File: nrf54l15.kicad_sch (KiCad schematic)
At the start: 16 parts, among them U1 nRF54L15-QDXX, X1 XL7EL89CKI-111YLC-32M

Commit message: Push current KiCad workspace changes
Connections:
- net I2C_SDA: now also U1.5 (P1.04); no longer U1.24 (P0.04)
- net PMIC_INT: now reaches U1.20 (P0.00)
- net VOUT1 renamed VOUT2
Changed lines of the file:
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@@
-	)
-	(no_connect
-		(at 109.22 88.9)
 	)
 	(no_connect
@@
 	)
 	(no_connect
+		(at 109.22 78.74)
+	)
+	(no_connect
 		(at 109.22 55.88)
 	)
@@
 	(wire
 		(pts
+			(xy 106.68 88.9) (xy 109.22 88.9)
+		)
+		(stroke
+			(width 0)
+			(type default)
+		)
+	)
+	(wire
+		(pts
 			(xy 101.6 71.12) (xy 109.22 71.12)
 		)
@@
 	(wire
 		(pts
+			(xy 82.55 63.5) (xy 106.68 63.5)
+		)
+		(stroke
+			(width 0)
+			(type default)
+		)
+	)
+	(wire
+		(pts
 			(xy 223.52 40.64) (xy 204.47 40.64)
 		)
@@
 	(wire
 		(pts
+			(xy 110.49 19.05) (xy 110.49 17.78)
+		)
+		(stroke
+			(width 0)
+			(type default)
+		)
+	)
+	(wire
+		(pts
 			(xy 191.77 30.48) (xy 191.77 29.21)
 		)
@@
 	(wire
 		(pts
+			(xy 106.68 68.58) (xy 109.22 68.58)
+		)
+		(stroke
+			(width 0)
+			(type default)
+		)
+	)
+	(wire
+		(pts
+			(xy 105.41 91.44) (xy 106.68 91.44)
+		)
+		(stroke
+			(width 0)
+			(type default)
+		)
+	)
+	(wire
+		(pts
 			(xy 165.1 93.98) (xy 172.72 93.98)
 		)
@@
 	(wire
 		(pts
+			(xy 106.68 91.44) (xy 106.68 88.9)
+		)
+		(stroke
+			(width 0)
+			(type default)
+		)
+	)
+	(wire
+		(pts
 			(xy 204.47 40.64) (xy 204.47 39.37)
 		)
@@
 	(wire
 		(pts
+			(xy 106.68 63.5) (xy 106.68 68.58)
+		)
+		(stroke
+			(width 0)
+			(type default)
+		)
+	)
+	(wire
+		(pts
 			(xy 186.69 93.98) (xy 186.69 97.79)
+		)
+		(stroke
+			(width 0)
+			(type default)
+		)
+	)
+	(wire
+		(pts
+			(xy 93.98 19.05) (xy 110.49 19.05)
 		)
 		(stroke
@@
 	(global_label "I2C_SDA"
 		(shape input)
-		(at 109.22 78.74 180)
+		(at 105.41 91.44 180)
 		(fields_autoplaced yes)
 		(effects
@@
 		)
 		(property "Intersheetrefs" "${INTERSHEET_REFS}"
-			(at 98.6148 78.74 0)
+			(at 94.8048 91.44 0)
 			(hide yes)
 			(show_name no)
@@
 		)
 	)
-	(global_label "VOUT1"
+	(global_label "nRF54_SWDCLK"
 		(shape input)
-		(at 110.49 17.78 180)
+		(at 165.1 142.24 0)
+		(fields_autoplaced yes)
+		(effects
+			(font
+				(size 1.27 1.27)
+			)
+			(justify left)
+		)
+		(property "Intersheetrefs" "${INTERSHEET_REFS}"
+			(at 182.4784 142.24 0)
+			(hide yes)
+			(show_name no)
+			(do_not_autoplace no)
+			(effects
+				(font
+					(size 1.27 1.27)
+				)
+				(justify left)
+			)
+		)
+	)
+	(global_label "nRF54_SWDIO"
+		(shape input)
+		(at 165.1 144.78 0)
+		(fields_autoplaced yes)
+		(effects
+			(font
+				(size 1.27 1.27)
+			)
+			(justify left)
+		)
+		(property "Intersheetrefs" "${INTERSHEET_REFS}"
+			(at 180.8456 144.78 0)
+			(hide yes)
+			(show_name no)
+			(do_not_autoplace no)
+			(effects
+				(font
+					(size 1.27 1.27)
+				)
+				(justify left)
+			)
+		)
+	)
+	(global_label "nRF54_RESET"
+		(shape input)
+		(at 190.5 137.16 0)
+		(fields_autoplaced yes)
+		(effects
+			(font
+				(size 1.27 1.27)
+			)
+			(justify left)
+		)
+		(property "Intersheetrefs" "${INTERSHEET_REFS}"
+			(at 206.1245 137.16 0)
+			(hide yes)
+			(show_name no)
+			(do_not_autoplace no)
+			(effects
+				(font
+					(size 1.27 1.27)
+				)
+				(justify left)
+			)
+		)
+	)
+	(global_label "ANT_SEL"
+		(shape output)
+		(at 101.6 71.12 180)
 		(fields_autoplaced yes)
 		(effects
@@
 		)
 		(property "Intersheetrefs" "${INTERSHEET_REFS}"
-			(at 101.5781 17.78 0)
+			(at 90.8739 71.12 0)
 			(hide yes)
 			(show_name no)
@@
 		)
 	)
-	(global_label "nRF54_SWDCLK"
+	(global_label "PMIC_INT"
 		(shape input)
-		(at 165.1 142.24 0)
-		(fields_autoplaced yes)
-		(effects
-			(font
-				(size 1.27 1.27)
-			)
-			(justify left)
-		)
-		(property "Intersheetrefs" "${INTERSHEET_REFS}"
-			(at 182.4784 142.24 0)
-			(hide yes)
-			(show_name no)
-			(do_not_autoplace no)
-			(effects
-				(font
-					(size 1.27 1.27)
-				)
-				(justify left)
-			)
-		)
-	)
-	(global_label "nRF54_SWDIO"
-		(shape input)
-		(at 165.1 144.78 0)
-		(fields_autoplaced yes)
-		(effects
-			(font
-				(size 1.27 1.27)
-			)
-			(justify left)
-		)
-		(property "Intersheetrefs" "${INTERSHEET_REFS}"
-			(at 180.8456 144.78 0)
-			(hide yes)
-			(show_name no)
-			(do_not_autoplace no)
-			(effects
-				(font
-					(size 1.27 1.27)
-				)
-				(justify left)
-			)
-		)
-	)
-	(global_label "nRF54_RESET"
-		(shape input)
-		(at 190.5 137.16 0)
-		(fields_autoplaced yes)
-		(effects
-			(font
-				(size 1.27 1.27)
-			)
-			(justify left)
-		)
-		(property "Intersheetrefs" "${INTERSHEET_REFS}"
-			(at 206.1245 137.16 0)
-			(hide yes)
-			(show_name no)
-			(do_not_autoplace no)
-			(effects
-				(font
-					(size 1.27 1.27)
-				)
-				(justify left)
-			)
-		)
-	)
-	(global_label "ANT_SEL"
-		(shape output)
-		(at 101.6 71.12 180)
+		(at 82.55 63.5 180)
 		(fields_autoplaced yes)
 		(effects
@@
 		)
 		(property "Intersheetrefs" "${INTERSHEET_REFS}"
-			(at 90.8739 71.12 0)
+			(at 71.0981 63.5 0)
 			(hide yes)
 			(show_name no)
@@
 			(hide yes)
 			(show_name no)
+			(do_not_autoplace no)
+			(effects
+				(font
+					(size 1.27 1.27)
+				)
+				(justify right)
+			)
+		)
+	)
+	(global_label "VOUT2"
+		(shape input)
+		(at 93.98 19.05 180)
+		(fields_autoplaced yes)
+		(effects
+			(font
+				(size 1.27 1.27)
+			)
+			(justify right)
+		)
+		(property "Intersheetrefs" "${INTERSHEET_REFS}"
+			(at 85.0681 19.05 0)
+			(hide yes)
+			(show_name no)

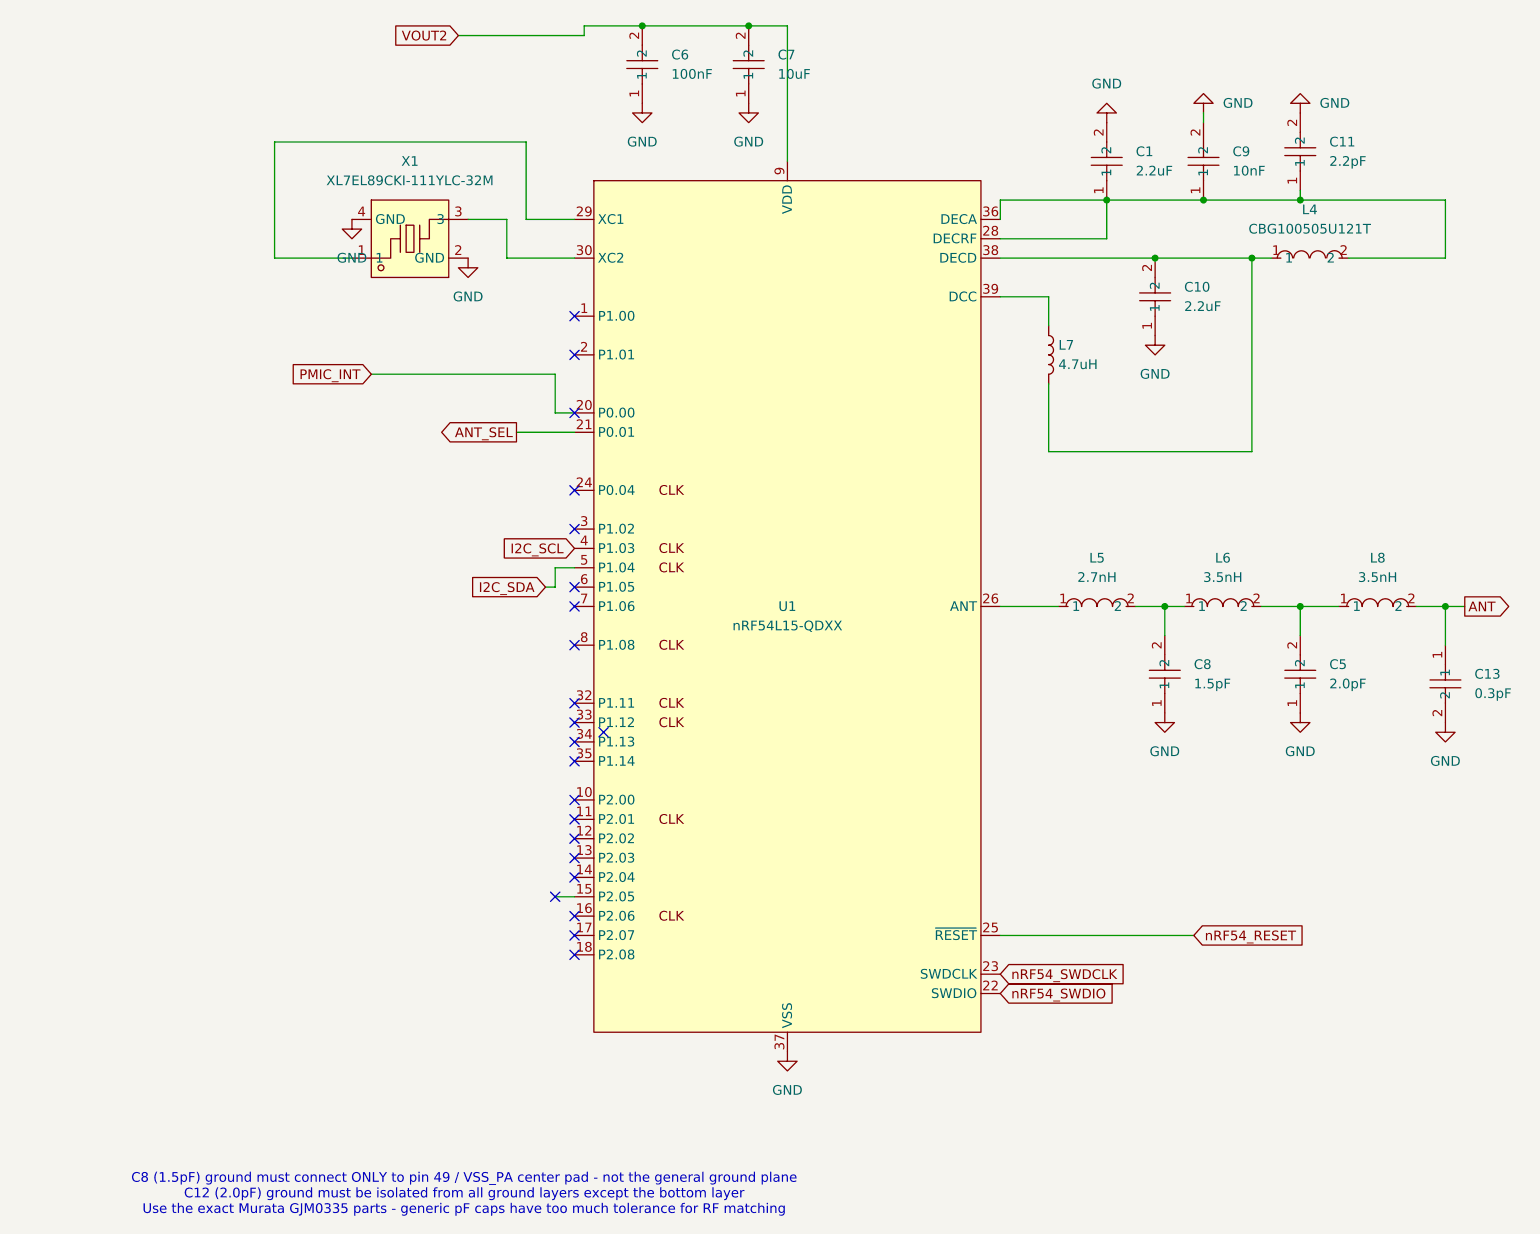
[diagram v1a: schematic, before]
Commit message: Update nRF54L15 schematic, PCB layout, and project configuration
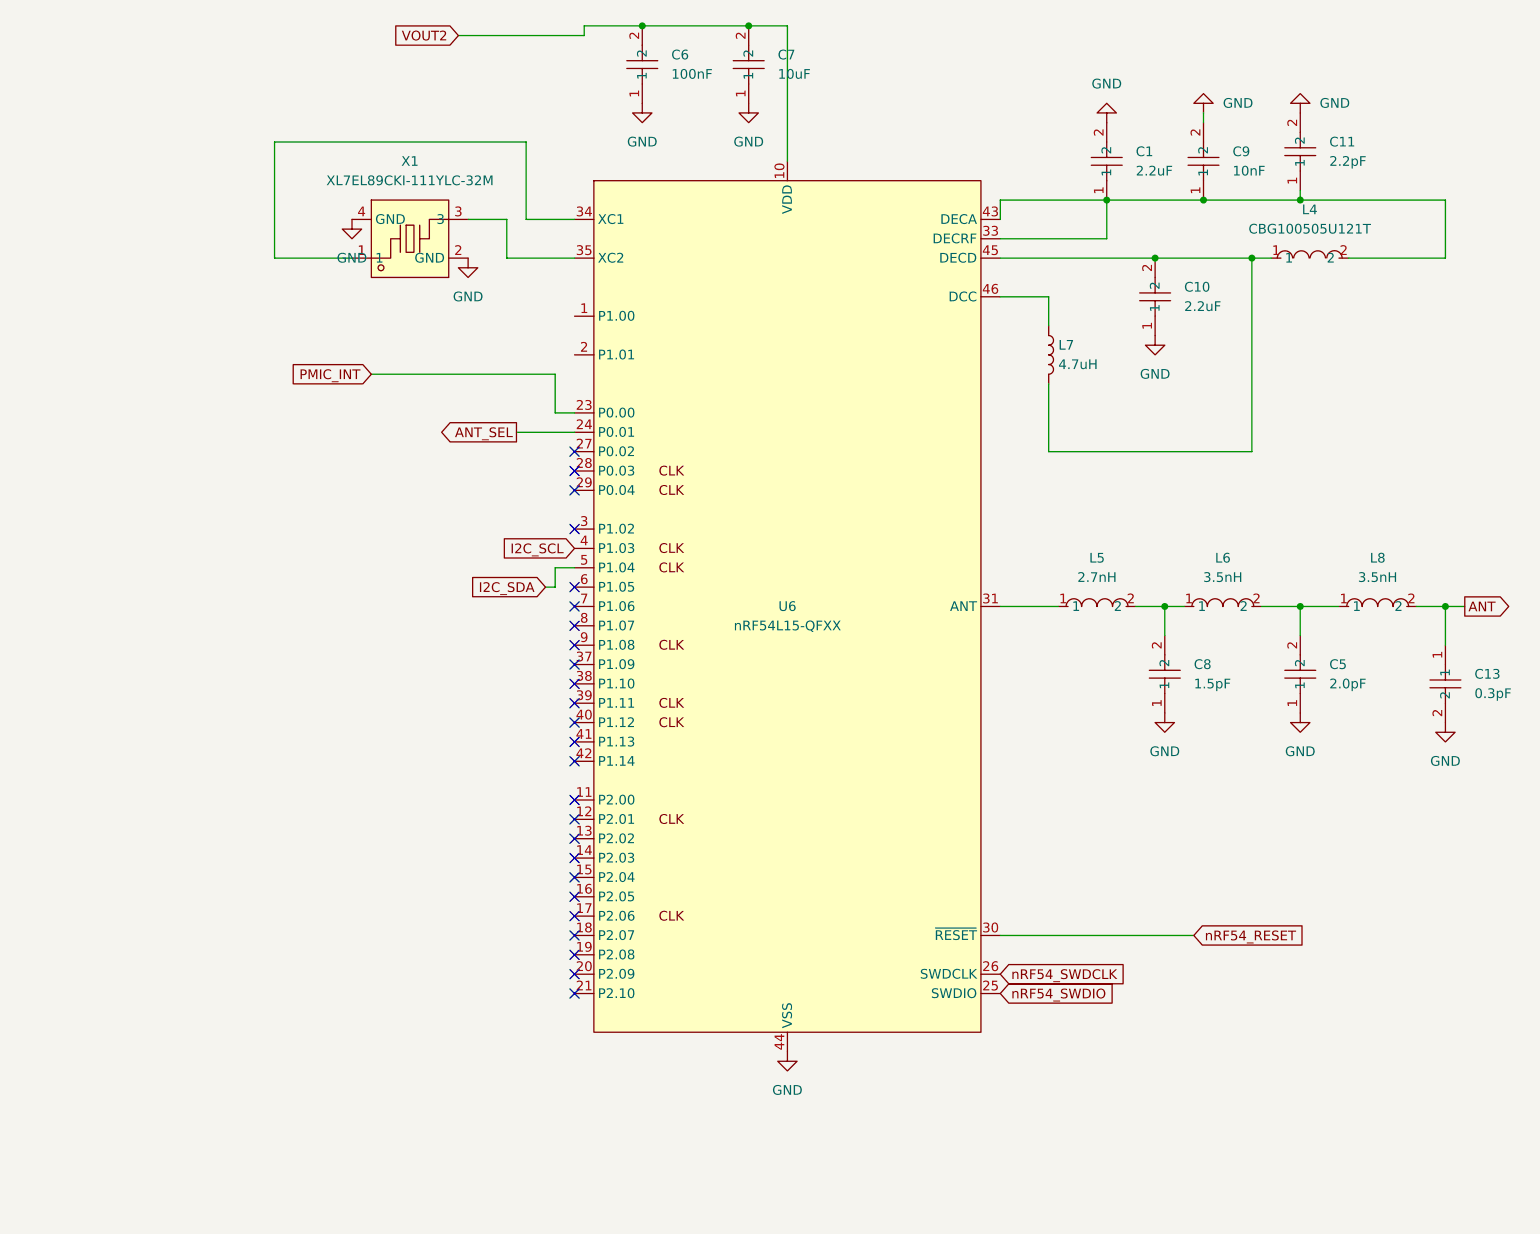
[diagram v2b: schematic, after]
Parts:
- removed U1: nRF54L15-QDXX, Package_DFN_QFN:QFN-40-1EP_5x5mm_P0.4mm_EP3.6x3.6mm_ThermalVias, symbol hlord2000:nRF54L15-QDXX
- added U6: nRF54L15-QFXX, Package_DFN_QFN:QFN-48-1EP_6x6mm_P0.4mm_EP4.6x4.6mm_ThermalVias, symbol hlord2000:nRF54L15-QFXX
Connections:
- net ANT_SEL: now also U6.24 (P0.01)
- net GND: now also U6.32 (VSS_PA), U6.44 (VSS), U6.49 (VSS)
- net I2C_SCL: now also U6.4 (P1.03)
- net I2C_SDA: now also U6.5 (P1.04)
- net PMIC_INT: now also U6.23 (P0.00)
- net VOUT2: now also U6.10 (VDD), U6.22 (VDD), U6.36 (VDD), U6.47 (VDD), U6.48 (VDD)
- net nRF54_RESET: now also U6.30 (~{RESET})
- net nRF54_SWDCLK: now also U6.26 (SWDCLK)
- net nRF54_SWDIO: now also U6.25 (SWDIO)
- net at C1.1, C11.1, C9.1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: now also U6.33 (DECRF), U6.43 (DECA)
- net at C10.2, L4.1, L7.2: now also U6.45 (DECD)
- net at X1.1: now also U6.34 (XC1)
- net at X1.3: now also U6.35 (XC2)
- net at L7.1: now also U6.46 (DCC)
- net at L5.1: now also U6.31 (ANT)
- no-connect marks 22 -> 25
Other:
- note removed: "C8 (1.5pF) ground must connect ONLY to pin 49 / VSS_PA center pad - not the general ground plane C12 (2.0pF) ground must be isolated from all ground layers except the bottom layer Use the exact Murata GJM0335 parts - generic pF caps have too much tolerance for RF matching"
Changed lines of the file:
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@@
 	(generator_version "10.0")
 	(paper "A4")
-	(text "C8 (1.5pF) ground must connect ONLY to pin 49 / VSS_PA center pad - not the general ground plane\nC12 (2.0pF) ground must be isolated from all ground layers except the bottom layer\nUse the exact Murata GJM0335 parts - generic pF caps have too much tolerance for RF matching"
-		(exclude_from_sim no)
-		(at 94.742 171.196 0)
-		(effects
-			(font
-				(size 1.27 1.27)
-			)
-		)
-	)
 	(junction
 		(at 185.42 48.26)
@@
 	)
 	(no_connect
-		(at 109.22 137.16)
+		(at 109.22 101.6)
 	)
 	(no_connect
-		(at 109.22 124.46)
+		(at 109.22 83.82)
 	)
 	(no_connect
-		(at 106.68 132.08)
+		(at 109.22 124.46)
 	)
 	(no_connect
-		(at 109.22 111.76)
+		(at 109.22 121.92)
 	)
 	(no_connect
-		(at 109.22 127)
+		(at 109.22 76.2)
 	)
 	(no_connect
-		(at 109.22 68.58)
+		(at 109.22 73.66)
 	)
 	(no_connect
-		(at 109.22 99.06)
+		(at 109.22 132.08)
 	)
 	(no_connect
-		(at 109.22 109.22)
+		(at 109.22 96.52)
 	)
 	(no_connect
-		(at 109.22 119.38)
+		(at 109.22 111.76)
 	)
 	(no_connect
-		(at 109.22 134.62)
+		(at 109.22 104.14)
 	)
 	(no_connect
-		(at 109.22 114.3)
+		(at 109.22 139.7)
 	)
 	(no_connect
-		(at 109.22 121.92)
+		(at 109.22 78.74)
 	)
 	(no_connect
-		(at 109.22 129.54)
+		(at 109.22 134.62)
 	)
 	(no_connect
-		(at 109.22 83.82)
+		(at 109.22 99.06)
 	)
 	(no_connect
@@
 	)
 	(no_connect
-		(at 109.22 139.7)
+		(at 109.22 119.38)
 	)
 	(no_connect
-		(at 113.03 110.49)
+		(at 109.22 114.3)
 	)
 	(no_connect
@@
 	)
 	(no_connect
-		(at 109.22 78.74)
+		(at 109.22 129.54)
+	)
+	(no_connect
+		(at 109.22 144.78)
 	)
 	(no_connect
-		(at 109.22 55.88)
+		(at 109.22 137.16)
+	)
+	(no_connect
+		(at 109.22 142.24)
+	)
+	(no_connect
+		(at 109.22 127)
 	)
 	(no_connect
@@
 	)
 	(no_connect
-		(at 109.22 60.96)
+		(at 109.22 109.22)
 	)
 	(wire
@@
 	(wire
 		(pts
-			(xy 106.68 132.08) (xy 109.22 132.08)
-		)
-		(stroke
-			(width 0)
-			(type default)
-		)
-	)
-	(wire
-		(pts
 			(xy 171.45 64.77) (xy 171.45 73.66)
 		)
@@
 	)
 	(symbol
+		(lib_id "hlord2000:nRF54L15-QFXX")
+		(at 137.16 93.98 0)
+		(unit 1)
+		(body_style 1)
+		(exclude_from_sim no)
+		(in_bom yes)
+		(on_board yes)
+		(in_pos_files yes)
+		(dnp no)
+		(fields_autoplaced yes)
+		(property "Reference" "U6"
+			(at 137.16 93.98 0)
+			(show_name no)
+			(do_not_autoplace yes)
+			(effects
+				(font
+					(size 1.27 1.27)
+				)
+			)
+		)
+		(property "Value" "nRF54L15-QFXX"
+			(at 137.16 96.52 0)
+			(show_name no)
+			(do_not_autoplace yes)
+			(effects
+				(font
+					(size 1.27 1.27)
+				)
+			)
+		)
+		(property "Footprint" "Package_DFN_QFN:QFN-48-1EP_6x6mm_P0.4mm_EP4.6x4.6mm_ThermalVias"
+			(at 137.16 167.64 0)
+			(hide yes)
+			(show_name no)
+			(do_not_autoplace no)
+			(effects
+				(font
+					(size 1.27 1.27)
+				)
+			)
+		)
+		(property "Datasheet" "https://docs.nordicsemi.com/bundle/ps_nrf54L15"
+			(at 137.16 170.18 0)
+			(hide yes)
+			(show_name no)
+			(do_not_autoplace no)
+			(effects
+				(font
+					(size 1.27 1.27)
+				)
+			)
+		)
+		(property "Description" "nRF54L Dual Core Multiprotocol BLE SoC"
+			(at 137.16 165.1 0)
+			(hide yes)
+			(show_name no)
+			(do_not_autoplace no)
+			(effects
+				(font
+					(size 1.27 1.27)
+				)
+			)
+		)
+		(pin "8"
+		)
+		(pin "11"
+		)
+		(pin "33"
+		)
+		(pin "2"
+		)
+		(pin "9"
+		)
+		(pin "45"
+		)
+		(pin "34"
+		)
+		(pin "44"
+		)
+		(pin "35"
+		)
+		(pin "23"
+		)
+		(pin "25"
+		)
+		(pin "46"
+		)
+		(pin "43"
+		)
+		(pin "1"
+		)
+		(pin "24"
+		)
+		(pin "31"
+		)
+		(pin "32"
+		)
+		(pin "3"
+		)
+		(pin "27"
+		)
+		(pin "30"
+		)
+		(pin "4"
+		)
+		(pin "5"
+		)
+		(pin "6"
+		)
+		(pin "7"
+		)
+		(pin "10"
+		)
+		(pin "13"
+		)
+		(pin "15"
+		)
+		(pin "17"
+		)
+		(pin "18"
+		)
+		(pin "20"
+		)
+		(pin "14"
+		)
+		(pin "19"
+		)
+		(pin "12"
+		)
+		(pin "16"
+		)
+		(pin "21"
+		)
+		(pin "38"
+		)
+		(pin "49"
+		)
+		(pin "28"
+		)
+		(pin "22"
+		)
+		(pin "37"
+		)
+		(pin "48"
+		)
+		(pin "39"
+		)
+		(pin "29"
+		)
+		(pin "26"
+		)
+		(pin "36"
+		)
+		(pin "40"
+		)
+		(pin "41"
+		)
+		(pin "42"
+		)
+		(pin "47"
+		)
+		(instances
+			(project "nrf54l15_soil_moisture"
+				(path "/55da176d-6431-4d58-ada7-b89d931b1434/b8c2cb22-3394-480f-839f-380498977228"
+					(reference "U6")
+					(unit 1)
+				)
+			)
+		)
+	)
+	(symbol
 		(lib_id "power:GND")
 		(at 179.07 30.48 180)
@@
 					(unit 1)
 				)
-			)
-		)
-	)
-	(symbol
-		(lib_id "hlord2000:nRF54L15-QDXX")
-		(at 137.16 93.98 0)
-		(unit 1)
-		(body_style 1)
-		(exclude_from_sim no)
-		(in_bom yes)
-		(on_board yes)
-		(in_pos_files yes)
-		(dnp no)
-		(fields_autoplaced yes)
-		(property "Reference" "U1"
-			(at 137.16 93.98 0)
-			(show_name no)
-			(do_not_autoplace yes)
-			(effects
-				(font
-					(size 1.27 1.27)
-				)
-			)
-		)
-		(property "Value" "nRF54L15-QDXX"
-			(at 137.16 96.52 0)
-			(show_name no)
-			(do_not_autoplace yes)
-			(effects
-				(font
-					(size 1.27 1.27)
-				)
-			)
-		)
-		(property "Footprint" "Package_DFN_QFN:QFN-40-1EP_5x5mm_P0.4mm_EP3.6x3.6mm_ThermalVias"
-			(at 137.16 167.64 0)
-			(hide yes)
-			(show_name no)
-			(do_not_autoplace no)
-			(effects
-				(font
-					(size 1.27 1.27)
-				)
-			)
-		)
-		(property "Datasheet" "https://docs.nordicsemi.com/bundle/ps_nrf54L15"
-			(at 137.16 170.18 0)
-			(hide yes)
-			(show_name no)
-			(do_not_autoplace no)
-			(effects
-				(font
-					(size 1.27 1.27)
-				)
-			)
-		)
-		(property "Description" "nRF54L Dual Core Multiprotocol BLE SoC"
-			(at 137.16 165.1 0)
-			(hide yes)
-			(show_name no)
-			(do_not_autoplace no)
-			(effects
-				(font
-					(size 1.27 1.27)
-				)
-			)
-		)
-		(pin "25"
-		)
-		(pin "4"
-		)
-		(pin "3"
-		)
-		(pin "6"
-		)
-		(pin "12"
-		)
-		(pin "20"
-		)
-		(pin "15"
-		)
-		(pin "16"
-		)
-		(pin "22"
-		)
-		(pin "21"
-		)
-		(pin "34"
-		)
-		(pin "2"
-		)
-		(pin "23"
-		)
-		(pin "9"
-		)
-		(pin "1"
-		)
-		(pin "10"
-		)
-		(pin "14"
-		)
-		(pin "18"
-		)
-		(pin "8"
-		)
-		(pin "30"
-		)
-		(pin "31"
-		)
-		(pin "7"
-		)
-		(pin "11"
-		)
-		(pin "27"
-		)
-		(pin "13"
-		)
-		(pin "19"
-		)
-		(pin "5"
-		)
-		(pin "17"
-		)
-		(pin "24"
-		)
-		(pin "26"
-		)
-		(pin "28"
-		)
-		(pin "29"
-		)
-		(pin "32"
-		)
-		(pin "33"
-		)
-		(pin "35"
-		)
-		(pin "36"
-		)
-		(pin "39"
-		)
-		(pin "40"
-		)
-		(pin "41"
-		)
-		(pin "37"
-		)
-		(pin "38"
-		)
-		(instances
-			(project "nrf54l15_soil_moisture"
-				(path "/55da176d-6431-4d58-ada7-b89d931b1434/b8c2cb22-3394-480f-839f-380498977228"
-					(reference "U1")
-					(unit 1)
-				)
